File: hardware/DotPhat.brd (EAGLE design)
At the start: 30 x 65 mm, 41 parts, among them CN1 1X4-BIG, IC1 CAT24M010TS, J2 RASPBERRYPI-40-PIN-GPIO_PTH, J3 USB-MICROB, U1 ATMEGA328P-MU-QFN32, U2 TMP102, U3 ATSHA204-TSU, X3 S4B-ZR

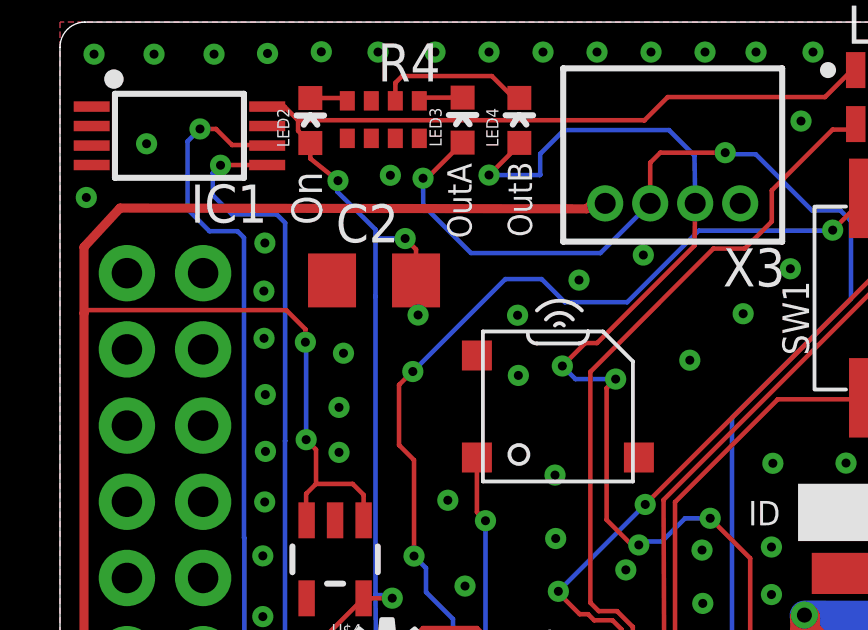
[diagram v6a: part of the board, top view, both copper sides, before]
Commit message: Correct short-circuit
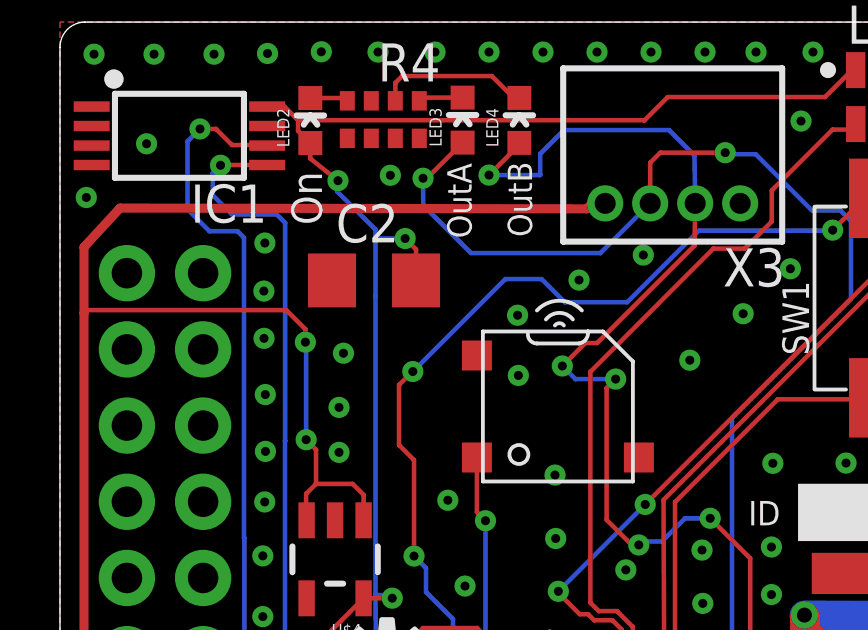
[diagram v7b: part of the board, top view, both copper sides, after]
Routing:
- net GND: vias 129 -> 128

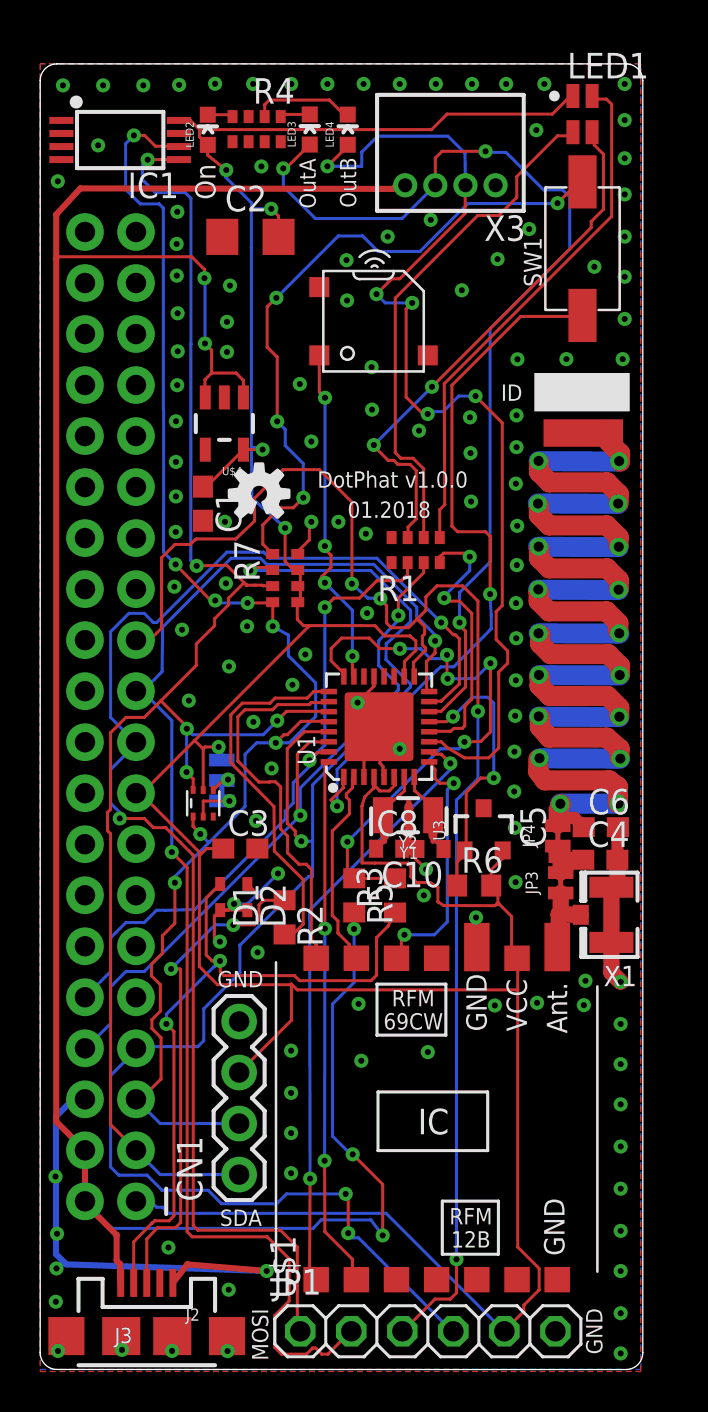
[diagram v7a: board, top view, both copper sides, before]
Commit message: Update USB pullup to downside, 3.3V instead of 5V
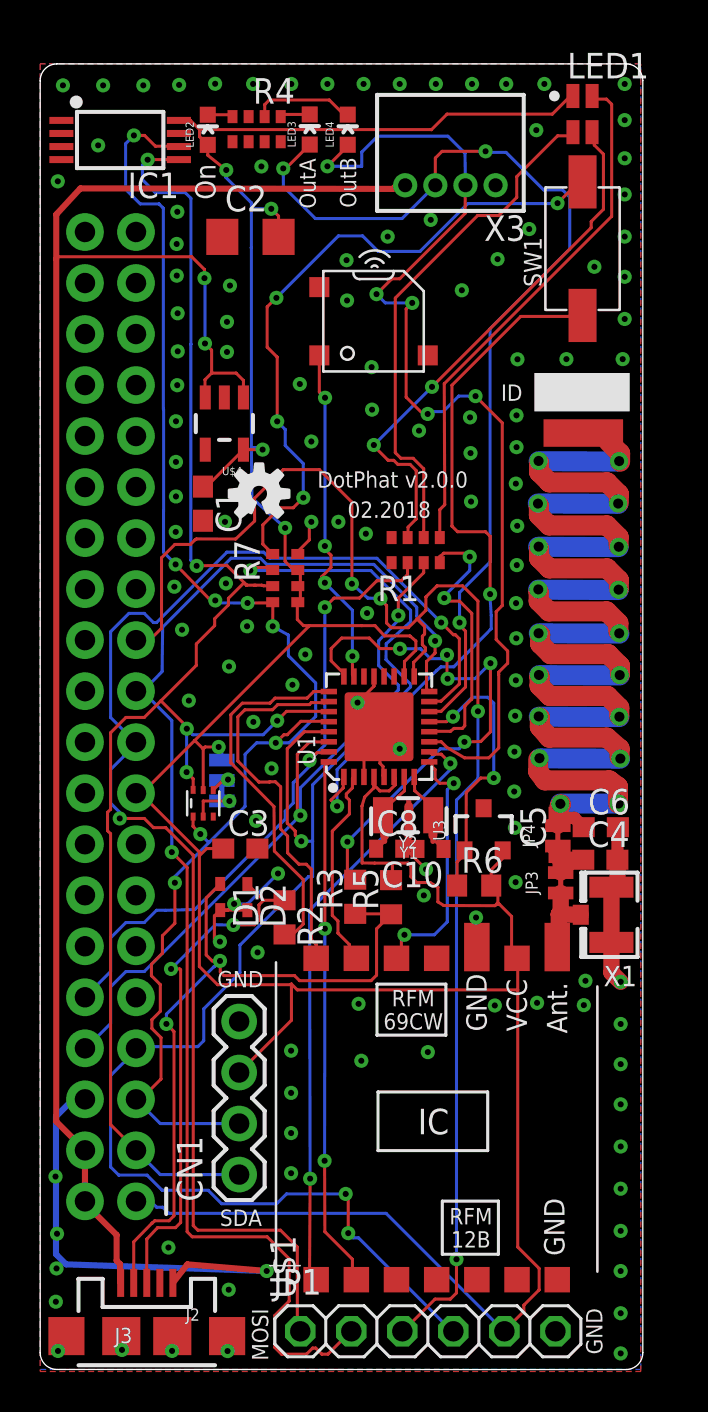
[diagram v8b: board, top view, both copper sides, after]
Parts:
- R2, R3: value (none) -> 68Ω
- R5: value (none) -> 1.5kΩ
- moved R3 1.98 mm to (15.7, 23.5)
- moved R5 1.84 mm to (17.5, 23.5), turned to 90 degrees
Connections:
- net +3V3: now also R5.2
- net +5V: no longer R5.2
- net D-: no longer R5.1
- net USB_D-: now also R5.1
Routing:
- net +5V: track 123.9 -> 90.3 mm, vias 5 -> 2
- net D-: track 28.8 -> 26.8 mm
- net USB_D-: track 35.3 -> 36.9 mm
- net +3V3: track 174.9 -> 175.8 mm
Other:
- board text added: "02.2018"
- board text added: "DotPhat v2.0.0"
- board text removed: "01.2018"
- board text removed: "DotPhat v1.0.0"
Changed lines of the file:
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@@
 <layer number="21" name="tPlace" color="7" fill="1" visible="yes" active="yes"/>
 <layer number="22" name="bPlace" color="7" fill="1" visible="yes" active="yes"/>
-<layer number="23" name="tOrigins" color="15" fill="1" visible="no" active="yes"/>
+<layer number="23" name="tOrigins" color="15" fill="1" visible="yes" active="yes"/>
 <layer number="24" name="bOrigins" color="15" fill="1" visible="no" active="yes"/>
 <layer number="25" name="tNames" color="7" fill="1" visible="no" active="yes"/>
@@
 <text x="11.355296875" y="0.44234375" size="0.8128" layer="21" rot="R90">MOSI</text>
 <text x="27.99045" y="0.7514625" size="0.8128" layer="21" rot="R90">GND</text>
-<text x="13.8" y="43.9" size="0.8128" layer="21">DotPhat v1.0.0</text>
-<text x="15.3" y="42.4" size="0.8128" layer="21">01.2018</text>
+<text x="13.8" y="43.9" size="0.8128" layer="21">DotPhat v2.0.0</text>
+<text x="15.3" y="42.4" size="0.8128" layer="21">02.2018</text>
 <rectangle x1="14" y1="28.7" x2="19.8" y2="34.9" layer="43"/>
 <rectangle x1="24.2" y1="20" x2="30" y2="49.9" layer="41"/>
@@
 <element name="D1" library="diode" package="SOD523" value="" x="8.96315625" y="23.5701875" rot="R270"/>
 <element name="D2" library="diode" package="SOD523" value="" x="10.31545" y="23.564596875" rot="R270"/>
-<element name="R2" library="rcl" package="R0603" value="" x="12.165075" y="22.508465625" rot="R270"/>
-<element name="R3" library="rcl" package="R0603" value="" x="17.663671875" y="23.598121875" rot="R90"/>
-<element name="R5" library="rcl" package="R0603" value="" x="15.635225" y="23.6037125" rot="R270"/>
+<element name="R2" library="rcl" package="R0603" value="68Ω" x="12.165075" y="22.508465625" rot="R270"/>
+<element name="R3" library="rcl" package="R0603" value="68Ω" x="15.683671875" y="23.533121875" rot="R90"/>
+<element name="R5" library="rcl" package="R0603" value="1.5kΩ" x="17.469775" y="23.5112875" rot="R90"/>
 <element name="IC1" library="CAT24M01YI" package="TSSOP8" value="CAT24M010TS" x="3.981446875" y="59.9396875">
 <attribute name="MF" value="On Semiconductor" x="-0.20116875" y="59.9396875" size="1.778" layer="27" display="off"/>
@@
 <via x="15.988240625" y="15.369725" extent="1-16" drill="0.3"/>
 <via x="27.590378125" y="54.897590625" extent="1-16" drill="0.3"/>
-<wire x1="11.935596875" y1="55.235665625" x2="11.935596875" y2="55.235665625" width="0" layer="19" extent="1-16"/>
 <via x="9.448934375" y="53.9616" extent="1-16" drill="0.3"/>
 <via x="0.87694375" y="59.152853125" extent="1-16" drill="0.3"/>
@@
 <wire x1="8.211565625" y1="30.991046875" x2="8.11656875" y2="30.89605" width="0.1524" layer="1"/>
 <wire x1="16.025875" y1="25.21635625" x2="16.64944375" y2="25.210265625" width="0.1524" layer="1"/>
-<wire x1="16.64944375" y1="25.210265625" x2="18.32305" y2="25.210265625" width="0.1524" layer="1"/>
+<wire x1="16.64944375" y1="25.210265625" x2="17.535" y2="25.210265625" width="0.1524" layer="1"/>
+<wire x1="17.535" y1="25.210265625" x2="18.32305" y2="25.210265625" width="0.1524" layer="1"/>
 <wire x1="18.32305" y1="25.210265625" x2="18.45436875" y2="25.070565625" width="0.1524" layer="1"/>
 <wire x1="18.45436875" y1="25.070565625" x2="18.45436875" y2="24.536909375" width="0.1524" layer="1"/>
@@
 <wire x1="11.505" y1="57.785" x2="10.5556" y2="57.785" width="0.1524" layer="16"/>
 <wire x1="10.5556" y1="57.785" x2="10.5156" y2="57.825" width="0.1524" layer="16"/>
+<contactref element="R5" pad="2"/>
+<wire x1="17.469775" y1="24.3612875" x2="17.535" y2="24.4265125" width="0.1524" layer="1" curve="90"/>
+<wire x1="17.535" y1="24.4265125" x2="17.535" y2="25.210265625" width="0.1524" layer="1"/>
 </signal>
 <signal name="ADCENA">
@@
 <wire x1="7.5438" y1="55.3974" x2="0.9016" y2="55.3974" width="0.1524" layer="1"/>
 <wire x1="0.9016" y1="55.3974" x2="0.8" y2="55.2958" width="0.1524" layer="1"/>
-<contactref element="R5" pad="2"/>
-<wire x1="15.635225" y1="22.7537125" x2="15.626840625" y2="22.7537125" width="0.1524" layer="1"/>
-<wire x1="15.626840625" y1="22.7537125" x2="15.626840625" y2="21.93010625" width="0.1524" layer="1"/>
-<via x="15.626840625" y="21.93010625" extent="1-16" drill="0.3"/>
-<wire x1="15.626840625" y1="21.93010625" x2="15.626840625" y2="19.264628125" width="0.1524" layer="16"/>
-<wire x1="15.626840625" y1="19.264628125" x2="14.553946875" y2="18.191734375" width="0.1524" layer="16"/>
-<wire x1="14.553946875" y1="18.191734375" x2="14.553946875" y2="11.617453125" width="0.1524" layer="16"/>
-<wire x1="3.56235" y1="7.024115625" x2="13.590015625" y2="7.024115625" width="0.1524" layer="16"/>
-<wire x1="13.590015625" y1="7.024115625" x2="13.99235" y2="7.446009375" width="0.1524" layer="16"/>
-<wire x1="13.99235" y1="7.446009375" x2="16.462246875" y2="7.446009375" width="0.1524" layer="16"/>
-<wire x1="16.462246875" y1="7.446009375" x2="17.05178125" y2="6.674865625" width="0.1524" layer="16"/>
-<via x="17.05178125" y="6.674865625" extent="1-16" drill="0.3"/>
-<wire x1="17.05178125" y1="6.674865625" x2="17.05178125" y2="9.217409375" width="0.1524" layer="1"/>
-<wire x1="17.05178125" y1="9.217409375" x2="15.5597875" y2="10.709403125" width="0.1524" layer="1"/>
-<via x="15.5597875" y="10.709403125" extent="1-16" drill="0.3"/>
-<wire x1="15.5597875" y1="10.709403125" x2="15.461996875" y2="10.709403125" width="0.1524" layer="16"/>
-<wire x1="15.461996875" y1="10.709403125" x2="14.553946875" y2="11.617453125" width="0.1524" layer="16"/>
-<wire x1="3.56235" y1="7.024115625" x2="3.56235" y2="7.03765" width="0.1524" layer="16"/>
-<wire x1="3.56235" y1="7.03765" x2="2.23" y2="8.37" width="0.1524" layer="16"/>
 <wire x1="2.23" y1="7.7306" x2="2.772046875" y2="7.7306" width="0.3048" layer="1"/>
 <wire x1="2.772046875" y1="7.7306" x2="3.805428125" y2="6.69721875" width="0.3048" layer="1"/>
@@
 <wire x1="8.264653125" y1="20.639278125" x2="8.264653125" y2="23.471684375" width="0.1524" layer="1"/>
 <wire x1="8.264653125" y1="23.471684375" x2="8.96315625" y2="24.1701875" width="0.1524" layer="1"/>
-<wire x1="17.663671875" y1="22.748121875" x2="17.3228" y2="22.07539375" width="0.1524" layer="1"/>
-<wire x1="17.3228" y1="22.07539375" x2="16.7472375" y2="21.49983125" width="0.1524" layer="1"/>
-<wire x1="16.7472375" y1="21.49983125" x2="16.7472375" y2="19.63064375" width="0.1524" layer="1"/>
+<wire x1="16.7472375" y1="21.93875" x2="16.7472375" y2="19.63064375" width="0.1524" layer="1"/>
 <wire x1="16.7472375" y1="19.63064375" x2="16.473425" y2="19.35683125" width="0.1524" layer="1"/>
 <wire x1="16.473425" y1="19.35683125" x2="12.91386875" y2="19.35683125" width="0.1524" layer="1"/>
@@
 <wire x1="8.965946875" y1="19.789903125" x2="8.965946875" y2="20.326346875" width="0.1524" layer="1"/>
 <wire x1="8.965946875" y1="20.326346875" x2="8.951975" y2="20.34031875" width="0.1524" layer="1"/>
+<contactref element="R5" pad="1"/>
+<wire x1="17.469775" y1="22.6612875" x2="17.447940625" y2="22.683121875" width="0.1524" layer="1" curve="90"/>
+<wire x1="17.447940625" y1="22.683121875" x2="15.683671875" y2="22.683121875" width="0.1524" layer="1"/>
+<wire x1="16.7472375" y1="21.93875" x2="17.469775" y2="22.6612875" width="0.1524" layer="1"/>
 </signal>
 <signal name="USB_D+">
@@
 <signal name="D-">
 <contactref element="R3" pad="2"/>
-<contactref element="R5" pad="1"/>
-<wire x1="17.663671875" y1="24.448121875" x2="15.635225" y2="24.448121875" width="0.1524" layer="1"/>
-<wire x1="15.635225" y1="24.448121875" x2="15.635225" y2="24.4537125" width="0.1524" layer="1"/>
 <wire x1="20.89353125" y1="31.25" x2="21.1226375" y2="31.2453" width="0.1524" layer="1"/>
 <via x="21.1226375" y="31.2453" extent="1-16" drill="0.3"/>
@@
 <wire x1="19.921221875" y1="30.898846875" x2="15.29435625" y2="26.27198125" width="0.1524" layer="16"/>
 <via x="15.29435625" y="26.27198125" extent="1-16" drill="0.3"/>
-<wire x1="15.29435625" y1="26.27198125" x2="15.29435625" y2="24.79458125" width="0.1524" layer="1"/>
-<wire x1="15.29435625" y1="24.79458125" x2="15.635225" y2="24.4537125" width="0.1524" layer="1"/>
 <contactref element="U1" pad="24"/>
 <wire x1="15.12" y1="34.5" x2="15.12" y2="34.646728125" width="0.1524" layer="1"/>
@@
 <wire x1="22.4162625" y1="31.745428125" x2="21.9329" y2="31.262065625" width="0.1524" layer="1"/>
 <wire x1="21.9329" y1="31.262065625" x2="21.1226375" y2="31.2453" width="0.1524" layer="1"/>
+<wire x1="15.635225" y1="24.448121875" x2="15.29435625" y2="24.788990625" width="0.1524" layer="1" curve="-90"/>
+<wire x1="15.29435625" y1="24.788990625" x2="15.29435625" y2="26.27198125" width="0.1524" layer="1"/>
+<wire x1="15.635225" y1="24.448121875" x2="15.683671875" y2="24.383121875" width="0" layer="19" extent="1-1"/>
 </signal>
 <signal name="D+">
